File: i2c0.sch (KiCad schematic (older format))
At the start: 12 parts, among them P8 PCA9685_OUT, U13 HMC5883L, U14 BME280, U15 2SMPB-02A

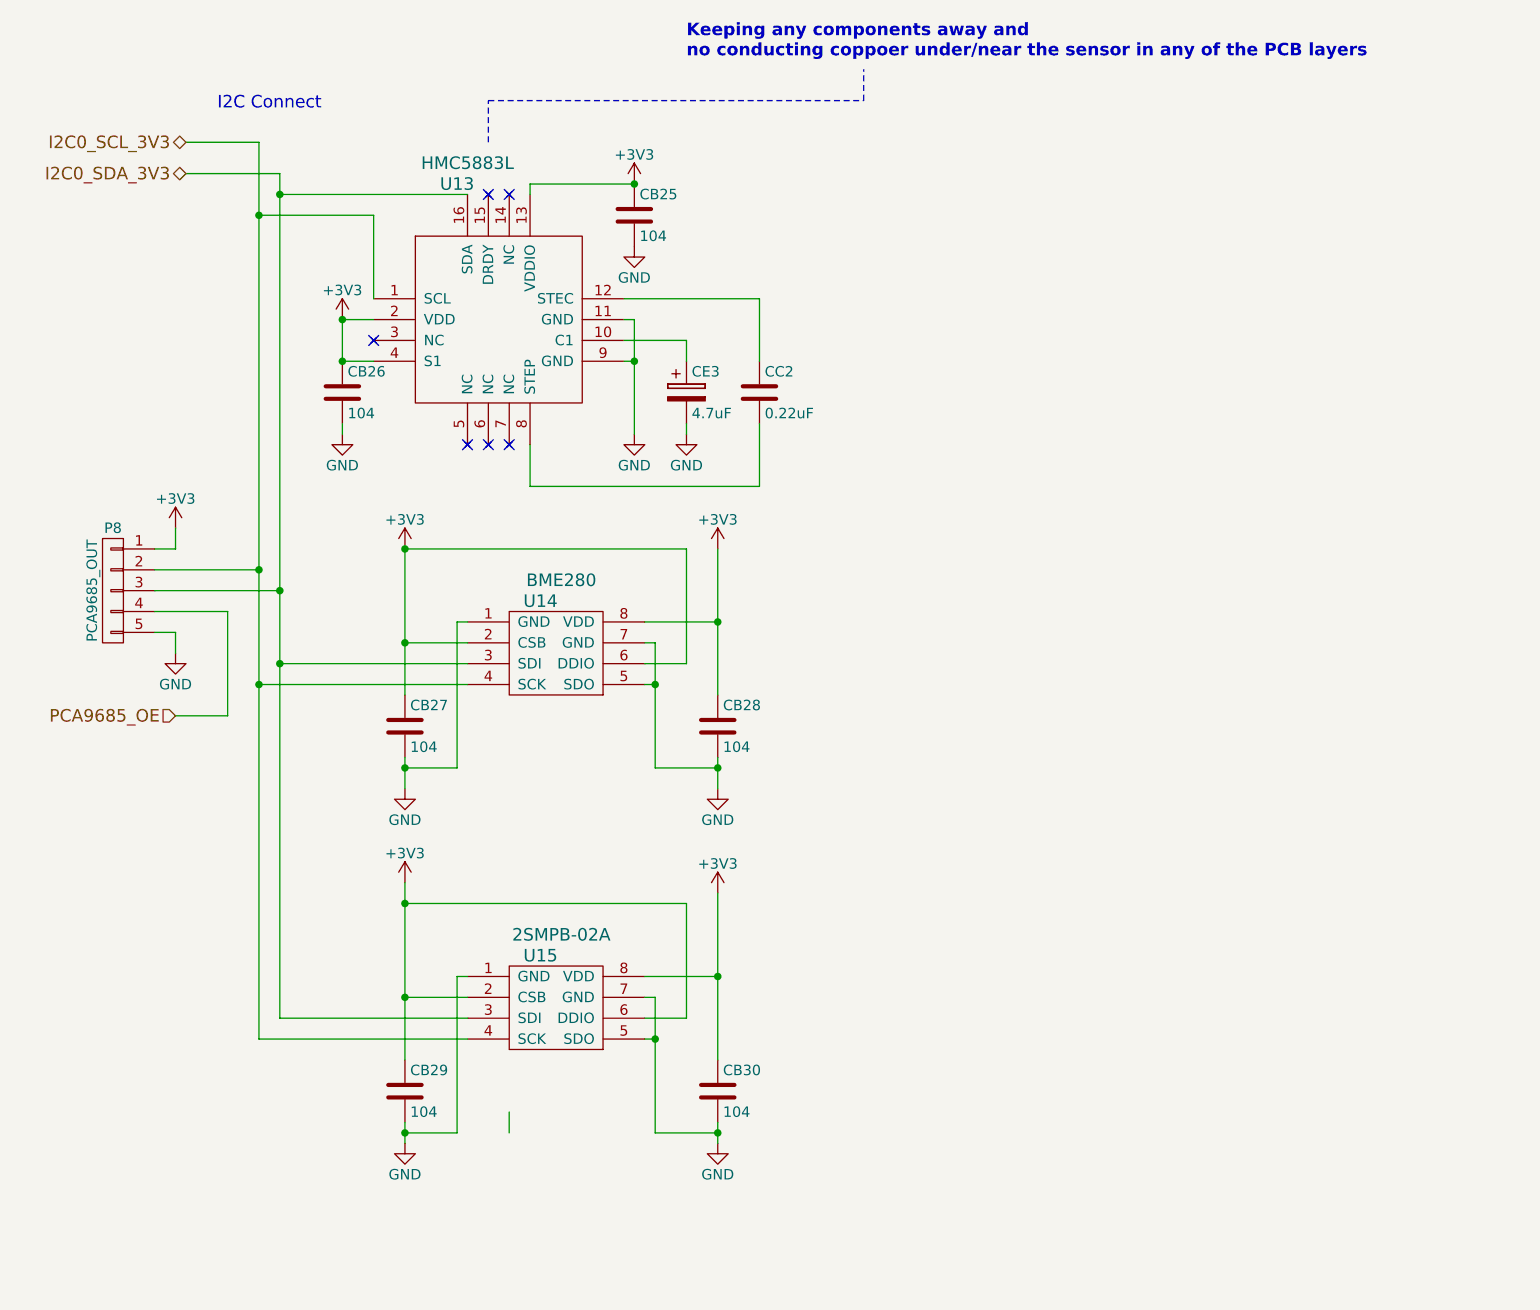
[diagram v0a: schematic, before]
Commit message: Improved the pin comatibility to match with other ardupilot project.
Signed-off-by: Akira Tsukamoto <akira-t@s9.dion.ne.jp>
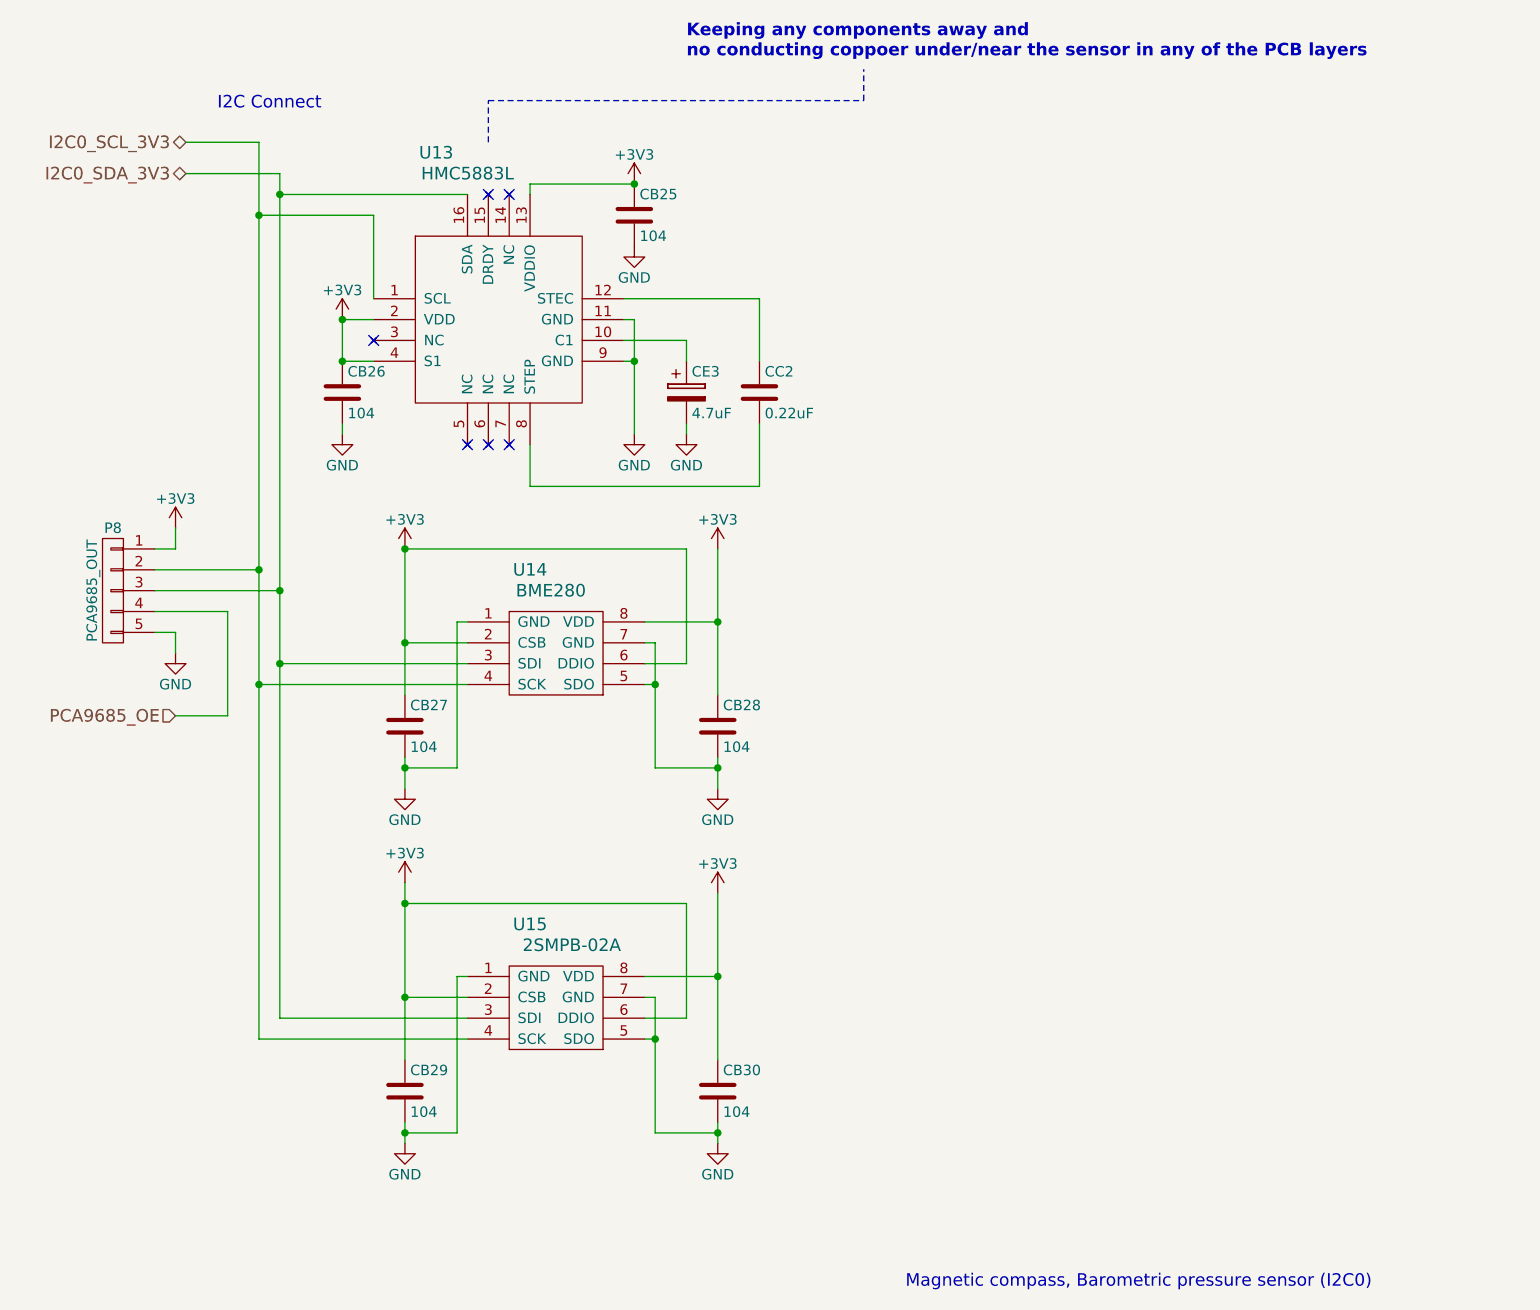
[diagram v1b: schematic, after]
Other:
- note added: "Magnetic compass, Barometric pressure sensor (I2C0)"
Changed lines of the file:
@@
 U 1 1 56F7AB4B
 P 5350 2850
-F 0 "U13" H 5150 3500 60  0000 C CNN
-F 1 "HMC5883L" H 5200 3600 60  0000 C CNN
+F 0 "U13" H 5050 3650 60  0000 C CNN
+F 1 "HMC5883L" H 5200 3550 60  0000 C CNN
 F 2 "droneworks:LPCC-16_HMC5883L_droneworks" H 5300 3500 60  0001 C CNN
 F 3 "" H 5300 3500 60  0000 C CNN
@@
 I2C Connect\n
 $Comp
-L GND #PWR073
+L GND #PWR075
 U 1 1 56F7AB57
 P 6400 5100
-F 0 "#PWR073" H 6400 4850 50  0001 C CNN
+F 0 "#PWR075" H 6400 4850 50  0001 C CNN
 F 1 "GND" H 6400 4950 50  0000 C CNN
 F 2 "" H 6400 5100 60  0000 C CNN
@@
 $EndComp
 $Comp
-L GND #PWR074
+L GND #PWR076
 U 1 1 56F7AB78
 P 6250 3400
-F 0 "#PWR074" H 6250 3150 50  0001 C CNN
+F 0 "#PWR076" H 6250 3150 50  0001 C CNN
 F 1 "GND" H 6250 3250 50  0000 C CNN
 F 2 "" H 6250 3400 60  0000 C CNN
@@
 $EndComp
 $Comp
-L GND #PWR075
+L GND #PWR077
 U 1 1 56F7AB93
 P 4600 3400
-F 0 "#PWR075" H 4600 3150 50  0001 C CNN
+F 0 "#PWR077" H 4600 3150 50  0001 C CNN
 F 1 "GND" H 4600 3250 50  0000 C CNN
 F 2 "" H 4600 3400 60  0000 C CNN
@@
 U 1 1 56FA4E05
 P 5650 4200
-F 0 "U14" H 5550 4200 60  0000 C CNN
-F 1 "BME280" H 5650 4300 60  0000 C CNN
+F 0 "U14" H 5500 4350 60  0000 C CNN
+F 1 "BME280" H 5600 4250 60  0000 C CNN
 F 2 "droneworks:LGA-8_BME280_droneworks" H 5650 4200 60  0001 C CNN
 F 3 "" H 5650 4200 60  0000 C CNN
@@
 $EndComp
 $Comp
-L +3V3 #PWR076
+L +3V3 #PWR078
 U 1 1 57076F4A
 P 4600 2850
-F 0 "#PWR076" H 4600 2700 50  0001 C CNN
+F 0 "#PWR078" H 4600 2700 50  0001 C CNN
 F 1 "+3V3" H 4600 2990 50  0000 C CNN
 F 2 "" H 4600 2850 50  0000 C CNN
@@
 $EndComp
 $Comp
-L +3V3 #PWR077
+L +3V3 #PWR079
 U 1 1 57076F6C
 P 6000 2200
-F 0 "#PWR077" H 6000 2050 50  0001 C CNN
+F 0 "#PWR079" H 6000 2050 50  0001 C CNN
 F 1 "+3V3" H 6000 2340 50  0000 C CNN
 F 2 "" H 6000 2200 50  0000 C CNN
@@
 $EndComp
 $Comp
-L +3V3 #PWR078
+L +3V3 #PWR080
 U 1 1 57076F8E
 P 4900 3950
-F 0 "#PWR078" H 4900 3800 50  0001 C CNN
+F 0 "#PWR080" H 4900 3800 50  0001 C CNN
 F 1 "+3V3" H 4900 4090 50  0000 C CNN
 F 2 "" H 4900 3950 50  0000 C CNN
@@
 U 1 1 573DACFE
 P 5650 5900
-F 0 "U15" H 5550 5900 60  0000 C CNN
-F 1 "2SMPB-02A" H 5650 6000 60  0000 C CNN
+F 0 "U15" H 5500 6050 60  0000 C CNN
+F 1 "2SMPB-02A" H 5700 5950 60  0000 C CNN
 F 2 "droneworks:LGA-8_2SMPB-02A_droneworks" H 5650 5900 60  0001 C CNN
 F 3 "" H 5650 5900 60  0000 C CNN
@@
 $EndComp
 $Comp
-L GND #PWR079
+L GND #PWR081
 U 1 1 573DAD05
 P 4900 6800
-F 0 "#PWR079" H 4900 6550 50  0001 C CNN
+F 0 "#PWR081" H 4900 6550 50  0001 C CNN
 F 1 "GND" H 4900 6650 50  0000 C CNN
 F 2 "" H 4900 6800 60  0000 C CNN
@@
 $EndComp
 $Comp
-L +3V3 #PWR080
+L +3V3 #PWR082
 U 1 1 573DAD33
 P 4900 5550
-F 0 "#PWR080" H 4900 5400 50  0001 C CNN
+F 0 "#PWR082" H 4900 5400 50  0001 C CNN
 F 1 "+3V3" H 4900 5690 50  0000 C CNN
 F 2 "" H 4900 5550 50  0000 C CNN
@@
 $EndComp
 $Comp
-L GND #PWR081
+L GND #PWR083
 U 1 1 58DE0591
 P 4900 5100
-F 0 "#PWR081" H 4900 4850 50  0001 C CNN
+F 0 "#PWR083" H 4900 4850 50  0001 C CNN
 F 1 "GND" H 4900 4950 50  0000 C CNN
 F 2 "" H 4900 5100 60  0000 C CNN
@@
 $EndComp
 $Comp
-L +3V3 #PWR082
+L +3V3 #PWR084
 U 1 1 58DE1D3E
 P 6400 3950
-F 0 "#PWR082" H 6400 3800 50  0001 C CNN
+F 0 "#PWR084" H 6400 3800 50  0001 C CNN
 F 1 "+3V3" H 6400 4090 50  0000 C CNN
 F 2 "" H 6400 3950 50  0000 C CNN
@@
 $EndComp
 $Comp
-L +3V3 #PWR083
+L +3V3 #PWR085
 U 1 1 58DE37C2
 P 6400 5600
-F 0 "#PWR083" H 6400 5450 50  0001 C CNN
+F 0 "#PWR085" H 6400 5450 50  0001 C CNN
 F 1 "+3V3" H 6400 5740 50  0000 C CNN
 F 2 "" H 6400 5600 50  0000 C CNN
@@
 $EndComp
 $Comp
-L GND #PWR084
+L GND #PWR086
 U 1 1 58DE3D1B
 P 6400 6800
-F 0 "#PWR084" H 6400 6550 50  0001 C CNN
+F 0 "#PWR086" H 6400 6550 50  0001 C CNN
 F 1 "GND" H 6400 6650 50  0000 C CNN
 F 2 "" H 6400 6800 60  0000 C CNN
@@
 	3850 2000 4200 2000
 Wire Wire Line
-	5400 6750 5400 6650
-Wire Wire Line
 	4300 6200 5200 6200
 Connection ~ 4300 4500
@@
 Connection ~ 4900 6100
 $Comp
-L GND #PWR085
+L GND #PWR087
 U 1 1 58DB55F7
 P 6000 2500
-F 0 "#PWR085" H 6000 2250 50  0001 C CNN
+F 0 "#PWR087" H 6000 2250 50  0001 C CNN
 F 1 "GND" H 6000 2350 50  0000 C CNN
 F 2 "" H 6000 2500 60  0000 C CNN
@@
 Connection ~ 6000 2200
 $Comp
-L GND #PWR086
+L GND #PWR088
 U 1 1 58DB5731
 P 6000 3400
-F 0 "#PWR086" H 6000 3150 50  0001 C CNN
+F 0 "#PWR088" H 6000 3150 50  0001 C CNN
 F 1 "GND" H 6000 3250 50  0000 C CNN
 F 2 "" H 6000 3400 60  0000 C CNN
@@
 	3700 4350 3800 4350
 $Comp
-L GND #PWR087
+L GND #PWR089
 U 1 1 56F7ABEC
 P 3800 4450
-F 0 "#PWR087" H 3800 4200 50  0001 C CNN
+F 0 "#PWR089" H 3800 4200 50  0001 C CNN
 F 1 "GND" H 3800 4300 50  0000 C CNN
 F 2 "" H 3800 4450 60  0000 C CNN
@@
 	3800 3950 3800 3850
 $Comp
-L +3V3 #PWR088
+L +3V3 #PWR090
 U 1 1 57076F28
 P 3800 3850
-F 0 "#PWR088" H 3800 3700 50  0001 C CNN
+F 0 "#PWR090" H 3800 3700 50  0001 C CNN
 F 1 "+3V3" H 3800 3990 50  0000 C CNN
 F 2 "" H 3800 3850 50  0000 C CNN
@@
 Text Notes 6250 1600 0    60   ~ 12
 Keeping any components away and \nno conducting coppoer under/near the sensor in any of the PCB layers
+Text Notes 7300 7500 0    60   ~ 0
+Magnetic compass, Barometric pressure sensor (I2C0)
 $EndSCHEMATC
